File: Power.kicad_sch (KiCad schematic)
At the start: 25 parts, among them J16 XT30, J17 Molex 470531000, Q1 DMP3013SFV-7, U11 EMC2301-1-ACZL-TR, U3 LMR33640DDDAR

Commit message: lots of changes, added usb power connections, gpio, hdmi, etc
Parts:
- TP1: footprint TestPoint:TestPoint_Pad_2.0x2.0mm -> Connector_PinHeader_2.00mm:PinHeader_1x01_P2.00mm_Vertical
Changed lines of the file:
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@@
 (kicad_sch (version 20201015) (generator eeschema)
-  (page 1 6)
+  (page 1 5)
   (paper "A4")
   (title_block
@@
   (junction (at 243.84 130.81) (diameter 1.016) (color 0 0 0 0))
   (junction (at 254 106.68) (diameter 1.016) (color 0 0 0 0))
+  (no_connect (at 71.755 169.545))
   (no_connect (at 161.29 111.76))
-  (no_connect (at 71.755 169.545))
   (no_connect (at 71.755 172.085))
   (wire (pts (xy 36.195 159.385) (xy 78.105 159.385))
@@
       (effects (font (size 1.27 1.27)) (justify left))
     )
-    (property "Footprint" "TestPoint:TestPoint_Pad_2.0x2.0mm" (id 2) (at 179.07 29.718 0)
+    (property "Footprint" "Connector_PinHeader_2.00mm:PinHeader_1x01_P2.00mm_Vertical" (id 2) (at 179.07 29.718 0)
       (effects (font (size 1.27 1.27)) hide)
     )

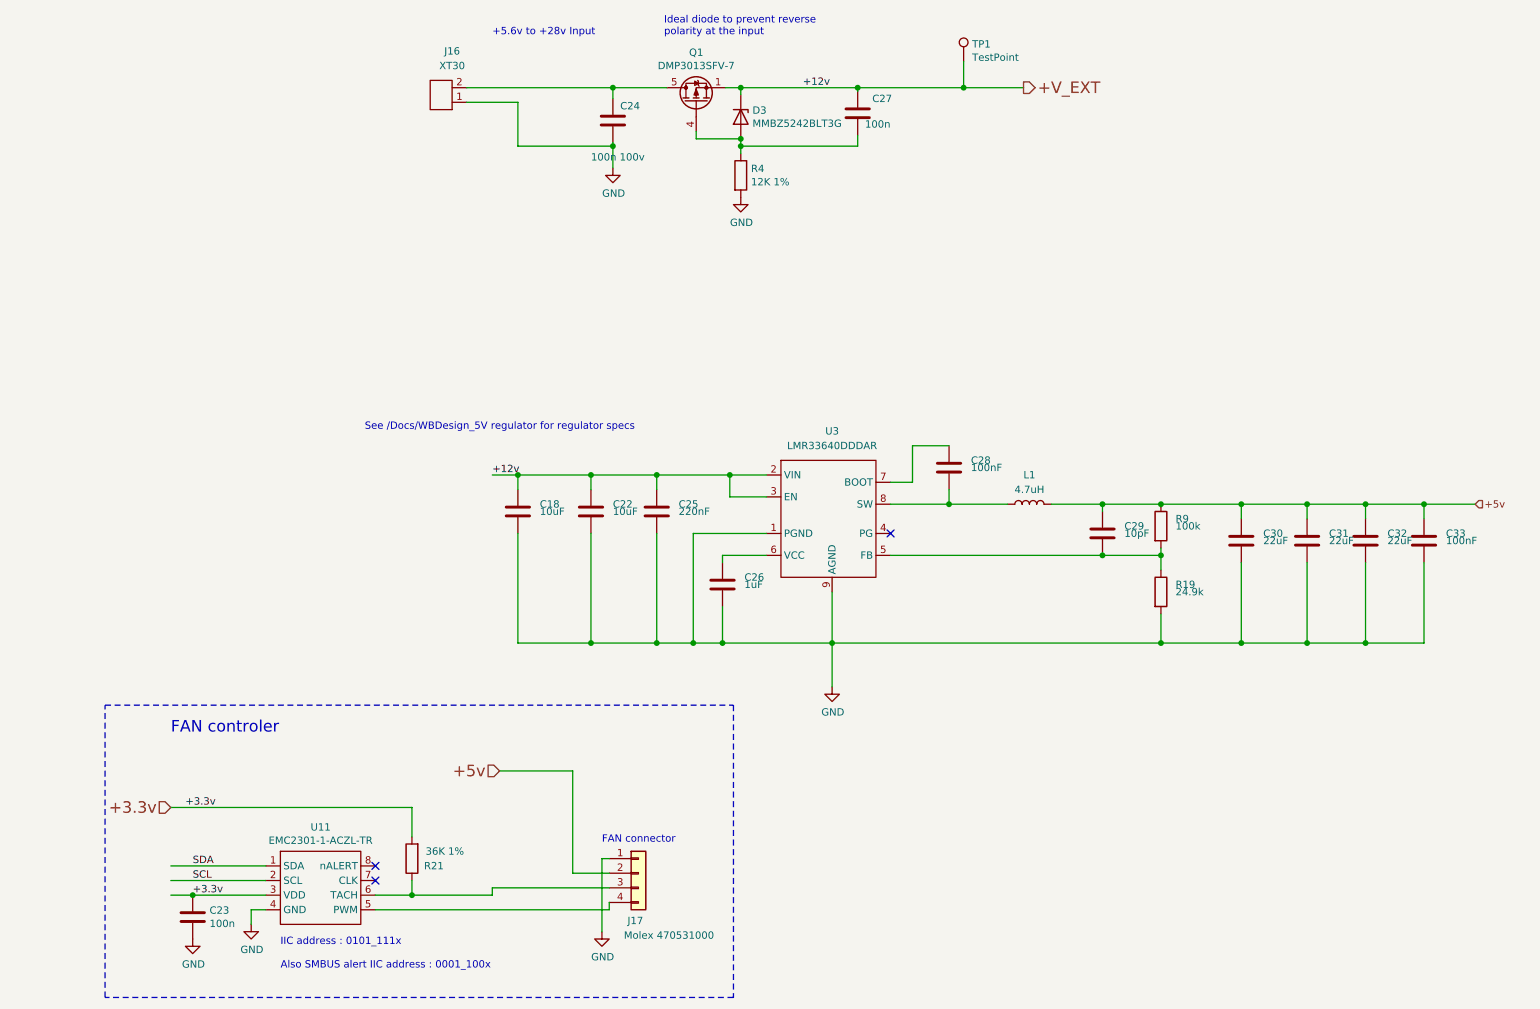
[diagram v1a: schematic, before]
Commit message: Changed footprint to match CM4, removed Ethernet and HDMI
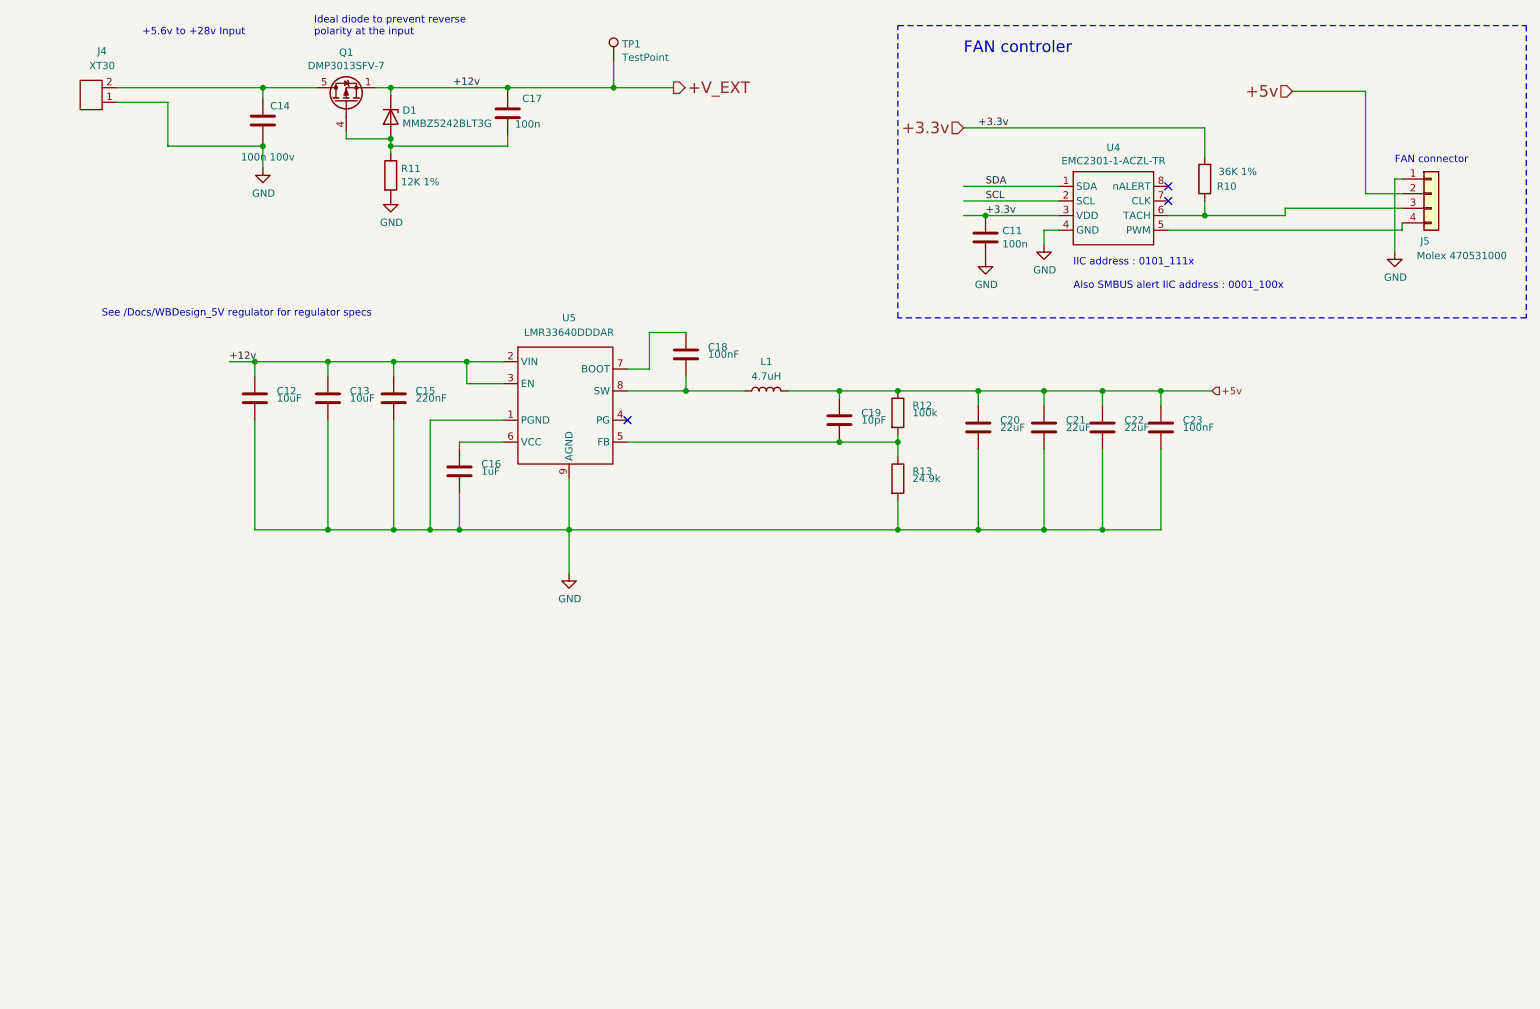
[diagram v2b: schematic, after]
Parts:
- renumbered C23 to C11, C18 to C12, C22 to C13, C24 to C14, C25 to C15, C26 to C16, C27 to C17, C28 to C18, C29 to C19, C30 to C20, C31 to C21, C32 to C22, C33 to C23, D3 to D1, J16 to J4, J17 to J5, R21 to R10, R4 to R11, R9 to R12, R19 to R13, U11 to U4, U3 to U5
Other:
- moved on the sheet: C11, C12, C13, C14, C15, C16, C17, C18, C19, C20, C21, C22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
